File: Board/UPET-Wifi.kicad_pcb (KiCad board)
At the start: 2 copper layers, 31.7 x 25.4 mm, 11 parts, among them U1 ESP32-C3-WROOM-02, U2 SC16IS752IPW, U3 1.8432 MHz

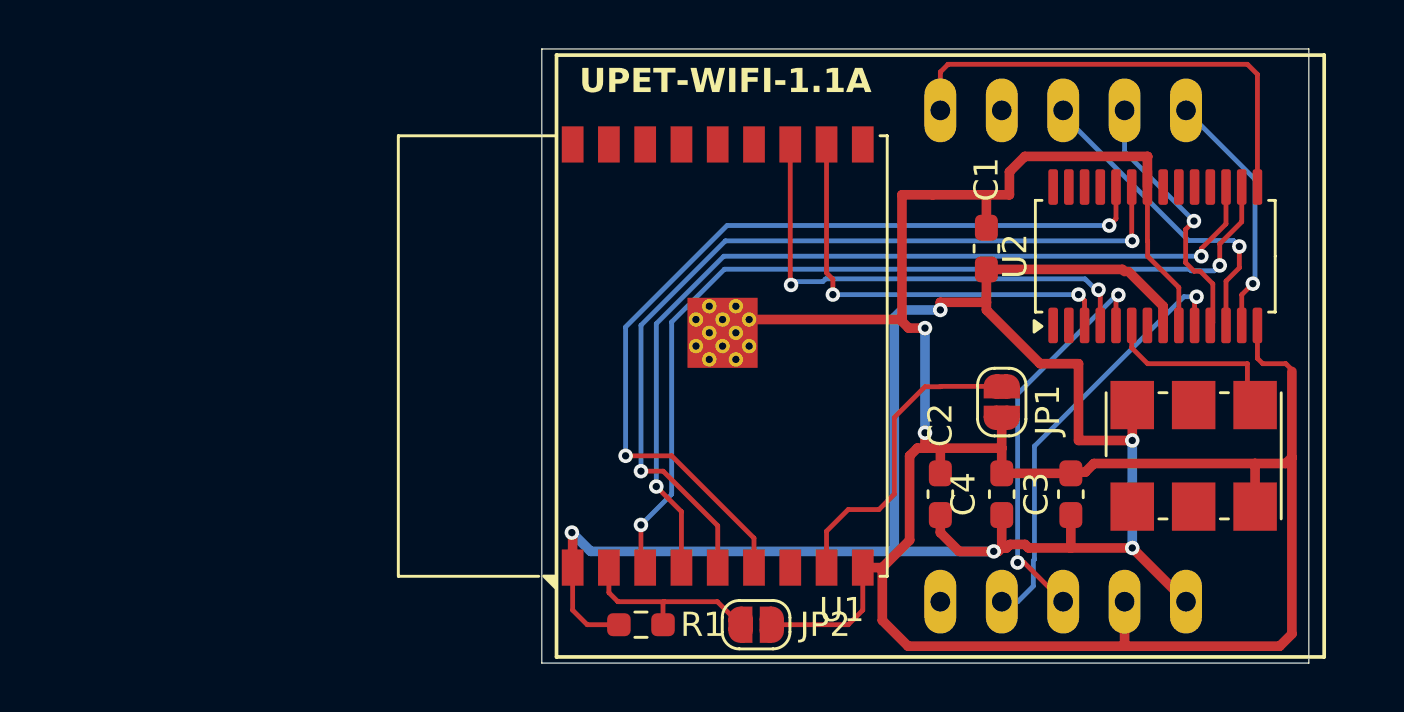
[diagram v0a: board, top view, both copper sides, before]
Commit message: move to 1.2 - separate serial prog interface
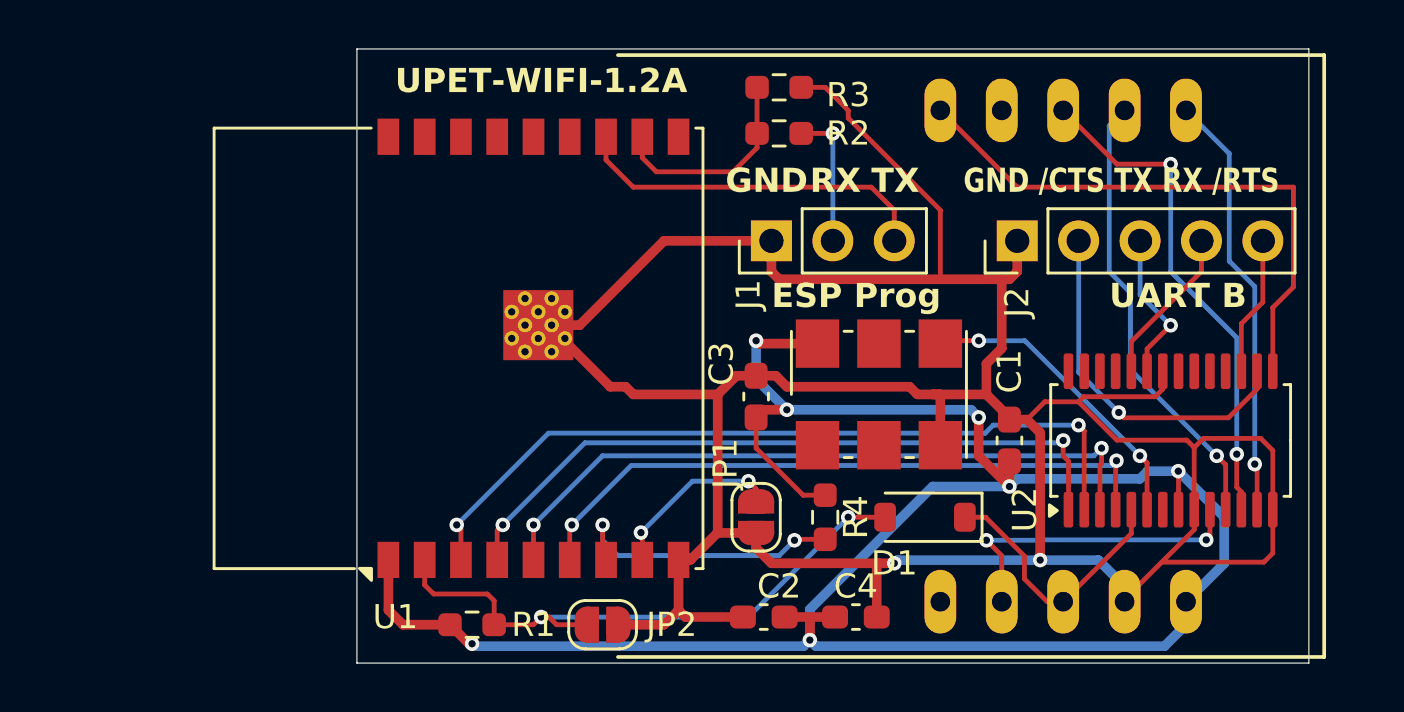
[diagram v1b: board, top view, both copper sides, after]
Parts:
- added D1: 1N4148W, Diode_SMD:D_SOD-123, F.Cu at (140.3, 101.9)
- added J1: Conn_01x03_Pin, Connector_PinHeader_2.54mm:PinHeader_1x03_P2.54mm_Vertical, F.Cu at (134.0, 90.5)
- added J2: Conn_01x05_Pin, Connector_PinHeader_2.54mm:PinHeader_1x05_P2.54mm_Vertical, F.Cu at (144.2, 90.5)
- added R2: 1k, Resistor_SMD:R_0603_1608Metric_Pad0.98x0.95mm_HandSolder, F.Cu at (134.3, 86.0)
- added R3: 1k5, Resistor_SMD:R_0603_1608Metric_Pad0.98x0.95mm_HandSolder, F.Cu at (134.3, 84.1)
- added R4: 10k, Resistor_SMD:R_0603_1608Metric_Pad0.98x0.95mm_HandSolder, F.Cu at (136.2, 101.9)
- moved C3 13.6 mm to (133.3, 96.9)
- moved U3 13.3 mm to (138.4, 96.8)
- moved JP1 11.2 mm to (133.3, 101.9)
- moved C2 8.90 mm to (133.7, 106.0), turned to 180 degrees
- moved C1 7.99 mm to (143.8, 98.7)
- moved C4 7.89 mm to (137.5, 106.0), turned to 0 degrees
- moved U2 7.65 mm to (150.5, 98.7)
- moved U1 7.63 mm to (124.1, 94.9)
- moved R1 6.98 mm to (121.6, 106.4)
- moved JP2 6.35 mm to (127.0, 106.4)
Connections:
- U1 pad 11: Net-(U1-IO20/RXD) -> /RXD
- U1 pad 12: Net-(U1-IO21/TXD) -> /TXD
- U1 pad 3: Net-(U1-IO4) -> //CTSA
- U1 pad 4: Net-(U1-IO5) -> //RTSA
- U1 pad 5: Net-(U1-IO6) -> /TXA
- U1 pad 6: Net-(U1-IO7) -> /RXA
- U1 pad 7: unconnected-(U1-IO8-Pad7) -> Net-(U1-IO8)
- U2 pad 1: unconnected-(U2-~{RTSA}-Pad1) -> //RTSA
- U2 pad 16: Net-(U1-IO4) -> //CTSB
- U2 pad 17: Net-(U1-IO5) -> //RTSB
- U2 pad 2: unconnected-(U2-~{CTSA}-Pad2) -> //CTSA
- U2 pad 23: Net-(U1-IO6) -> /TXB
- U2 pad 24: Net-(U1-IO7) -> /RXB
- U2 pad 3: Net-(U1-IO20/RXD) -> /TXA
- U2 pad 4: Net-(U1-IO21/TXD) -> /RXA
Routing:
- net Net-(U1-IO4): track 38.1 -> 0.00 mm, vias 2 -> 0
- net Net-(U1-IO5): track 37.5 -> 0.00 mm, vias 2 -> 0
- net Net-(U1-IO7): track 36.7 -> 0.00 mm, vias 2 -> 0
- net Net-(U1-IO6): track 35.9 -> 0.00 mm, vias 2 -> 0
- net GND: track 106.4 -> 140.1 mm
- net //CTSA: track 0.00 -> 32.5 mm, vias 0 -> 2
- net //RTSA: track 0.00 -> 29.1 mm, vias 0 -> 2
- net /TXA: track 0.00 -> 28.8 mm, vias 0 -> 2
- net /RXA: track 0.00 -> 27.1 mm, vias 0 -> 2
- net Net-(U1-IO21/TXD): track 20.3 -> 0.00 mm, vias 2 -> 0
- net Net-(U1-IO20/RXD): track 17.9 -> 0.00 mm, vias 2 -> 0
- net Net-(D1-A): track 7.99 -> 25.2 mm, vias 0 -> 2
- net /TXD: track 0.00 -> 15.0 mm
- net //CTSB: track 0.00 -> 14.8 mm, vias 0 -> 1
- net VCC: track 78.3 -> 92.7 mm, vias 5 -> 7
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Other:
- board size 31.7 x 25.4 mm -> 39.4 x 25.4 mm
- board text added: "ESP Prog"
- board text added: "GND"
- board text added: "GND /CTS TX RX /RTS"
- board text added: "RX"
- board text added: "TX"
- board text added: "UART B"
- board text added: "UPET-WIFI-1.2A"
- board text removed: "UPET-WIFI-1.1A"

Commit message: work on wifi 1.3a
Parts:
- removed J2: Conn_01x05_Pin, Connector_PinHeader_2.54mm:PinHeader_1x05_P2.54mm_Vertical
- added J3: Conn_01x09, Connector_PinHeader_2.54mm:PinHeader_1x09_P2.54mm_Vertical, F.Cu at (132.7, 89.7)
- added Q1: S8050, Package_TO_SOT_SMD:SOT-23, F.Cu at (127.9, 101.0)
- added Q2: S8050, Package_TO_SOT_SMD:SOT-23, F.Cu at (127.9, 95.8)
- added R5: 12k, Resistor_SMD:R_0603_1608Metric_Pad0.98x0.95mm_HandSolder, F.Cu at (128.0, 91.4)
- added R6: 12k, Resistor_SMD:R_0603_1608Metric_Pad0.98x0.95mm_HandSolder, F.Cu at (128.0, 88.1)
- J1: value Conn_01x03_Pin -> Conn_01x06; footprint Connector_PinHeader_2.54mm:PinHeader_1x03_P2.54mm_Vertical -> Connector_PinHeader_2.54mm:PinHeader_1x06_P2.54mm_Vertical
- moved JP1 9.20 mm to (141.2, 97.2), turned to 180 degrees
- moved R4 8.61 mm to (128.7, 106.0), turned to 0 degrees
- moved R1 6.79 mm to (114.8, 106.4)
- moved U1 6.79 mm to (117.3, 94.9)
- moved R3 6.33 mm to (128.0, 84.8)
- moved JP2 5.46 mm to (121.5, 106.6)
- moved U3 5.17 mm to (134.6, 100.3)
- moved J1 2.13 mm to (132.7, 92.2)
- moved C3 1.33 mm to (132.7, 95.8), turned to 0 degrees
- moved R2 1.13 mm to (134.0, 85.0)
- moved D1 1.03 mm to (141.1, 101.2), turned to -90 degrees
- moved U2 0.63 mm to (150.7, 99.3)
- moved C2 0.57 mm to (133.1, 106.0)
- moved C1 0.48 mm to (144.3, 98.9)
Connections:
- J1 pad 3: /TXD -> Net-(J1-Pin_3)
- R2 pad 2: Net-(J1-Pin_2) -> Net-(J1-Pin_3)
- U2 pad 18: unconnected-(U2-GPIO0/~{DSRB}-Pad18) -> //DSRB
- U2 pad 19: unconnected-(U2-GPIO1/~{DTRB}-Pad19) -> //DTRB
- U2 pad 20: unconnected-(U2-GPIO2/~{CDB}-Pad20) -> //CDB
- U2 pad 21: unconnected-(U2-GPIO3/~{RIB}-Pad21) -> //RIB
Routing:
- net Net-(J1-Pin_6): track 0.00 -> 29.3 mm, vias 0 -> 2
- net Net-(JP1-B): track 7.45 -> 27.3 mm, vias 2 -> 3
- net VCC: track 92.7 -> 74.7 mm, vias 7 -> 6
- net Net-(J1-Pin_2): track 5.75 -> 21.4 mm
- net Net-(Q1-B): track 0.00 -> 15.2 mm
- net /TXB: track 6.32 -> 20.6 mm
- net Net-(D1-A): track 25.2 -> 39.1 mm, vias 2 -> 3
- net //CTSB: track 14.8 -> 28.6 mm
- net //DSRB: track 0.00 -> 12.3 mm, vias 0 -> 2
- net //DTRB: track 0.00 -> 11.5 mm, vias 0 -> 2
- net //RTSB: track 5.76 -> 16.5 mm, vias 0 -> 1
- net //RIB: track 0.00 -> 9.80 mm, vias 0 -> 2
- net /TXD: track 15.0 -> 24.8 mm, vias 0 -> 1
- net GND: track 140.1 -> 130.8 mm, vias 2 -> 3
- net Net-(J1-Pin_3): track 0.00 -> 8.44 mm
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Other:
- board size 39.4 x 25.4 mm -> 45.8 x 25.4 mm
- board text added: "/CD"
- board text added: "/CTS"
- board text added: "/DSR"
- board text added: "/DTR"
- board text added: "/RI"
- board text added: "/RTS"
- board text added: "UPET-WIFI-1.3A"
- board text removed: "GND /CTS TX RX /RTS"
- board text removed: "UPET-WIFI-1.2A"
